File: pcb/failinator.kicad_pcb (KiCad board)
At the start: 2 copper layers, 200 x 124 mm, 68 parts, among them P1 CONN_01X04, P2 CONN_01X06, P3 CONN_01X06, P4 CONN_01X06, U1 74HC594, U2 RASPIPLUSHEADER, U3 LDS-CD16RI, U4 LDS-CD16RI, U5 74HC594

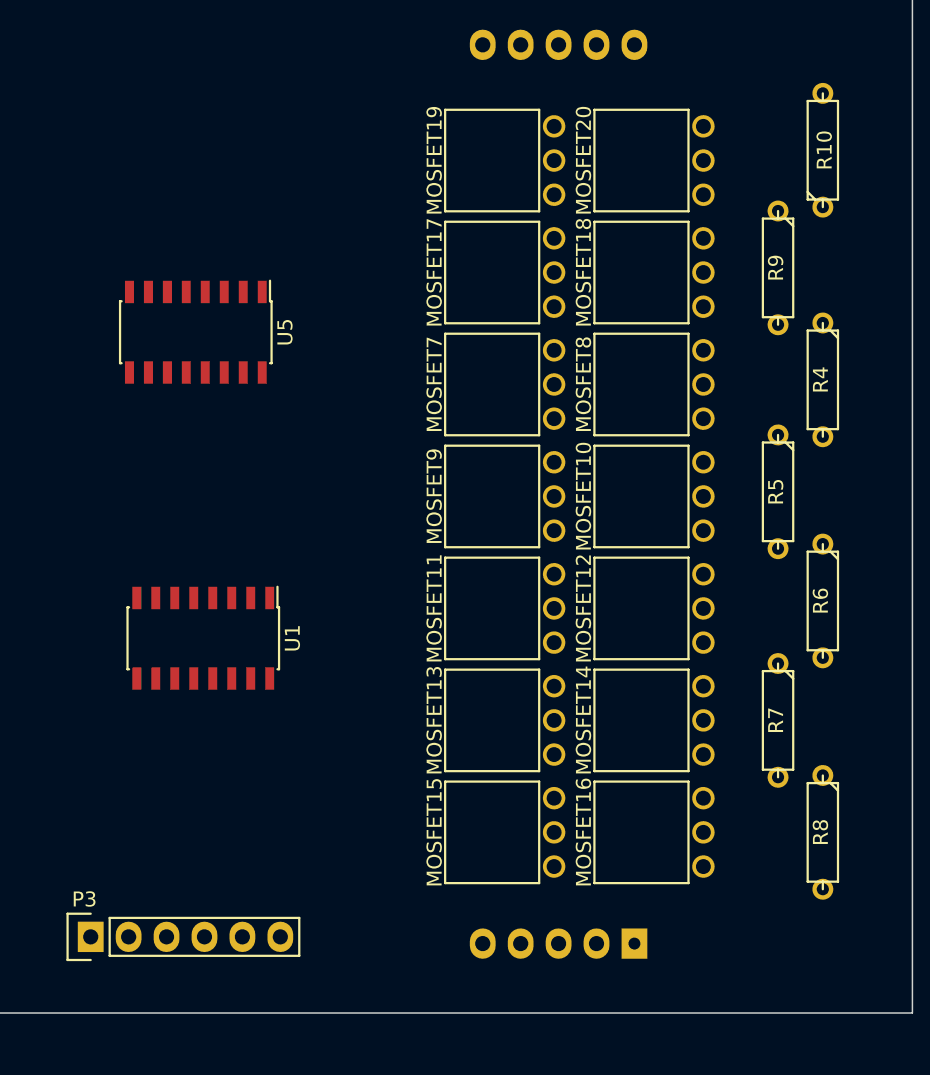
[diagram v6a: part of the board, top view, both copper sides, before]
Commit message: Initial work on traces for digit 0's MOSFETs
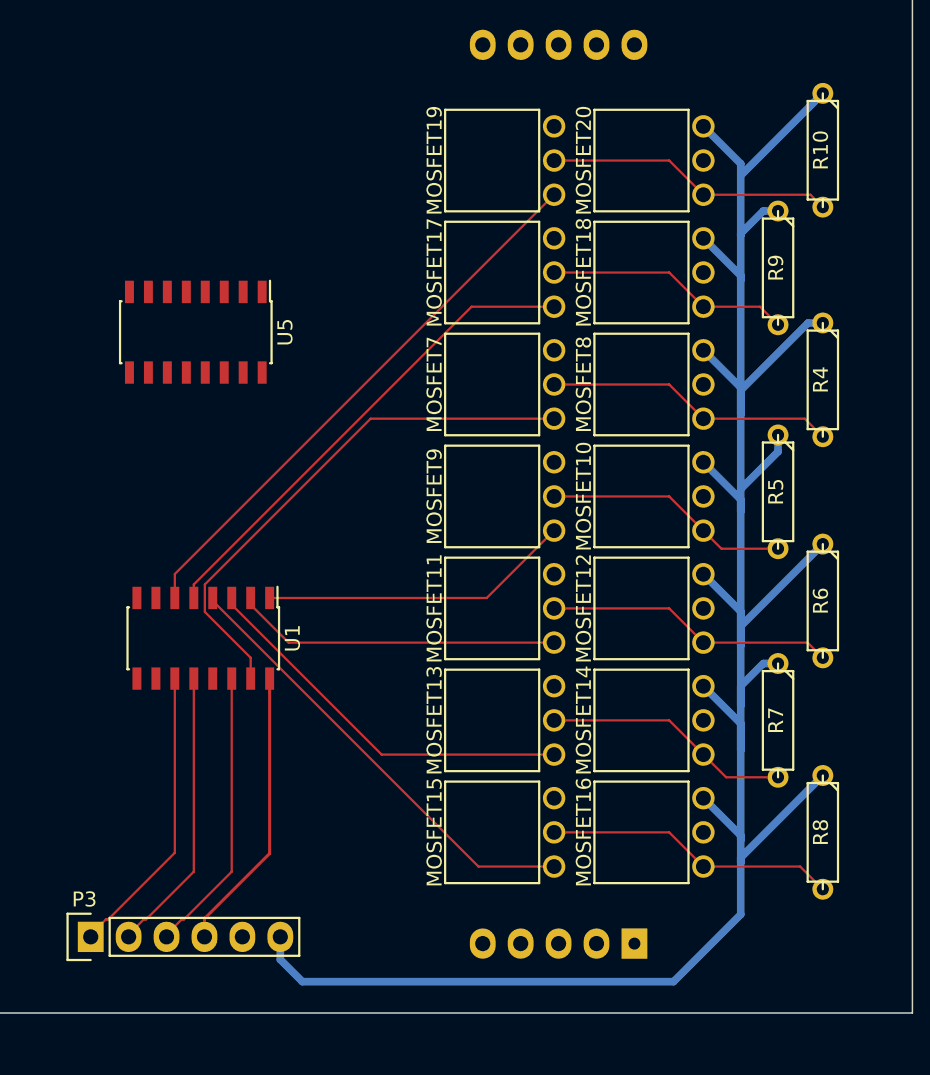
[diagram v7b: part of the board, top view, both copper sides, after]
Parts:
- turned R10 to 270 degrees
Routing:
- net /DisplayDrivers/VIN: track 0.00 -> 161.4 mm
- net /DisplayDrivers/G0_L: track 0.00 -> 37.5 mm
- net /DisplayDrivers/A0_L: track 0.00 -> 35.6 mm
- net /DisplayDrivers/F0_L: track 0.00 -> 32.7 mm
- net /DisplayDrivers/E0_L: track 0.00 -> 30.4 mm
- net /DisplayDrivers/D0_L: track 0.00 -> 26.2 mm
- net /DisplayDrivers/C0_L: track 0.00 -> 21.8 mm
- net /DisplayDrivers/B0_L: track 0.00 -> 20.9 mm
- net /D_SCLK: track 0.00 -> 19.7 mm
- net Net-(MOSFET15-Pad2): track 0.00 -> 19.6 mm
- net Net-(MOSFET7-Pad2): track 0.00 -> 19.4 mm
- net Net-(MOSFET11-Pad2): track 0.00 -> 19.4 mm
- net Net-(MOSFET19-Pad2): track 0.00 -> 19.3 mm
- net /D_MOSI: track 0.00 -> 19.2 mm
- net /D_DISP_CS: track 0.00 -> 19.2 mm
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
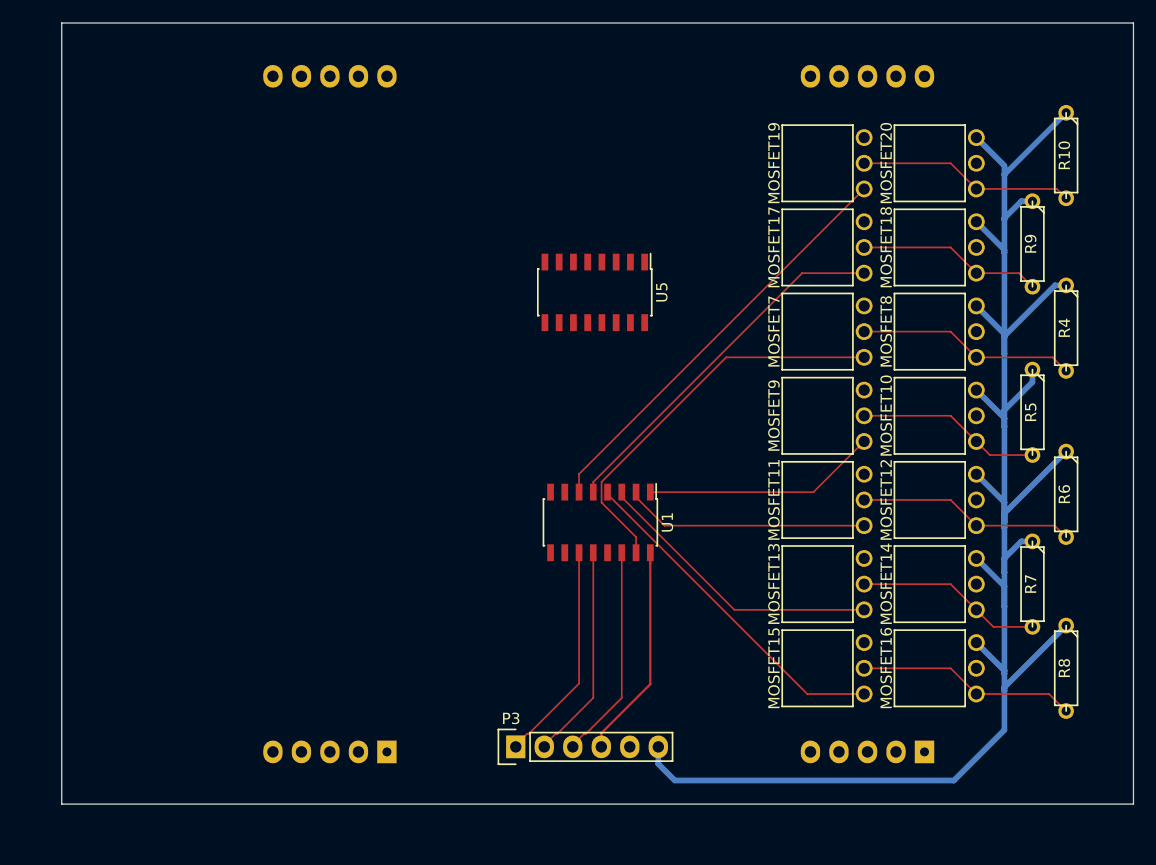
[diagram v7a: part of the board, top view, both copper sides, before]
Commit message: Ground plane for the LED display board
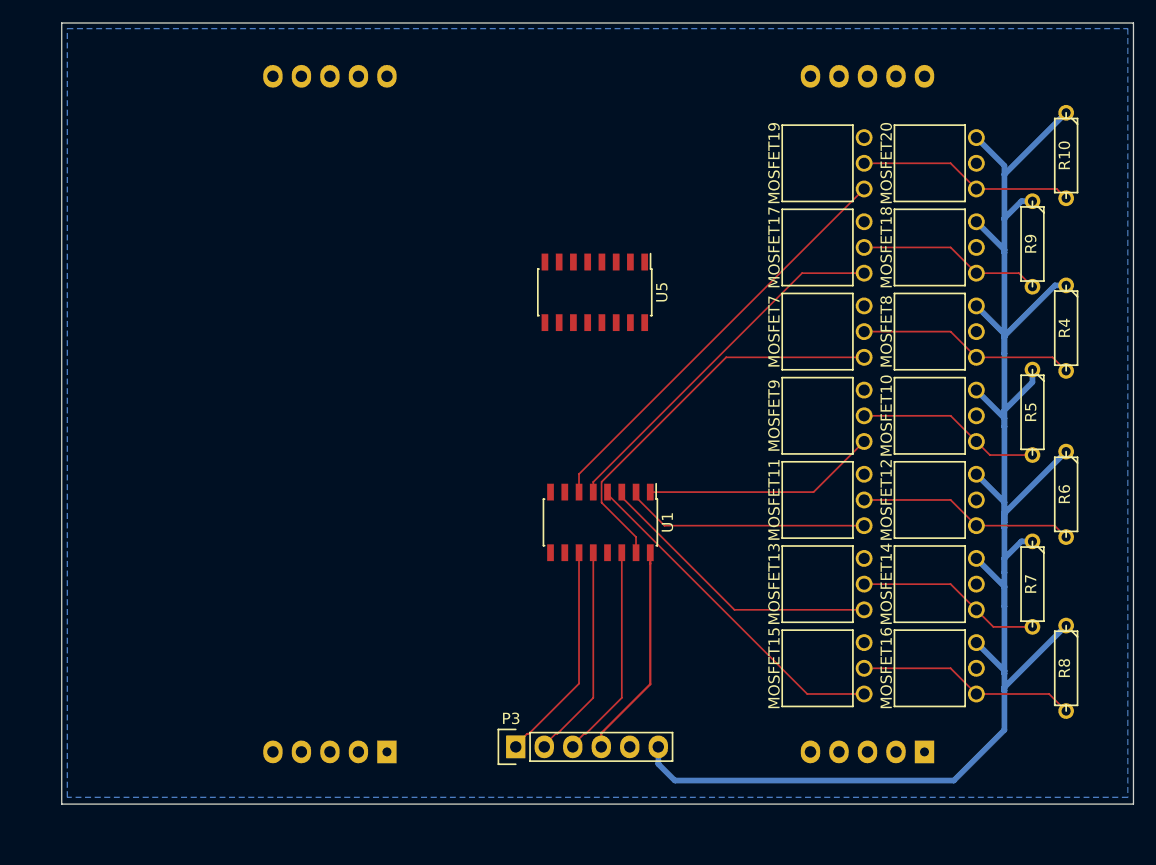
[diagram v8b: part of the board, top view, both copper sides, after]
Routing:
- added copper zone on B.Cu, net /DisplayDrivers/GND
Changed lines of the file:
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@@
+    )
+  )
+  (zone (net 38) (net_name /DisplayDrivers/GND) (layer B.Cu) (hatch edge 0.508)
+    (connect_pads (clearance 0.508))
+    (min_thickness 0.254)
+    (fill yes (arc_segments 16) (thermal_gap 0.508) (thermal_bridge_width 0.508))
+    (polygon
+      (pts
+        (xy 200.5 0.5) (xy 295 0.5) (xy 295 69) (xy 200.5 69)
+      )
     )
   )
